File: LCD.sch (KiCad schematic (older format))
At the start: 5 parts

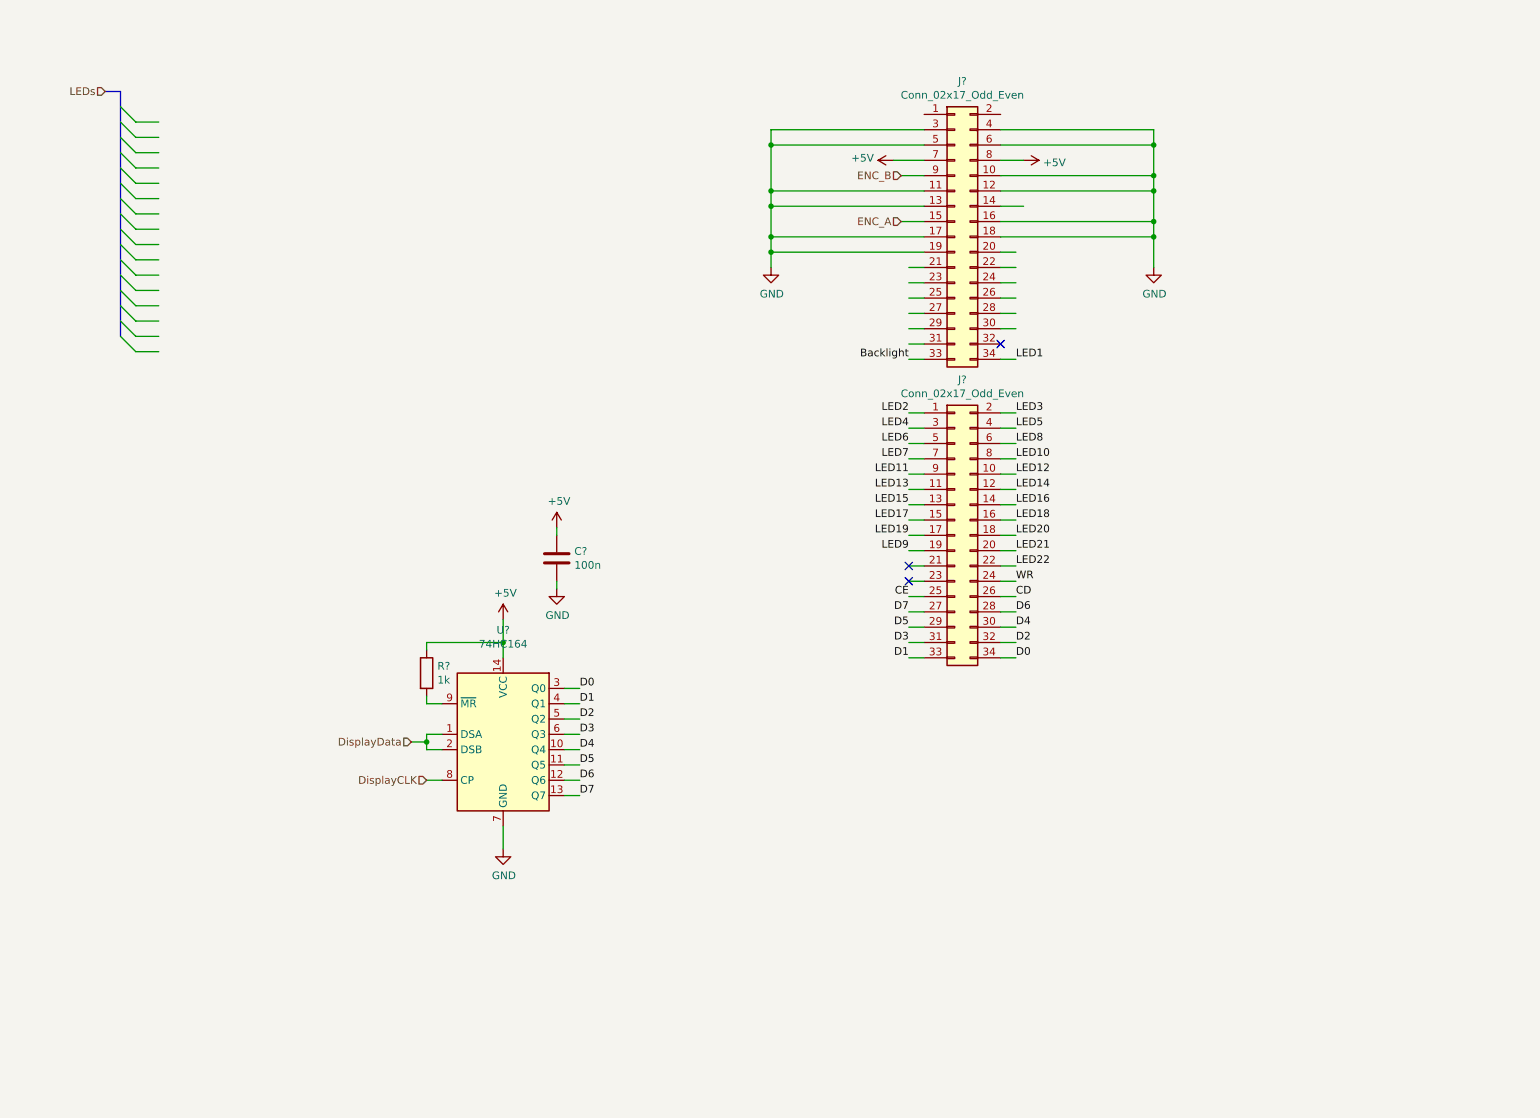
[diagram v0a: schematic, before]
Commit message: added rj45 input
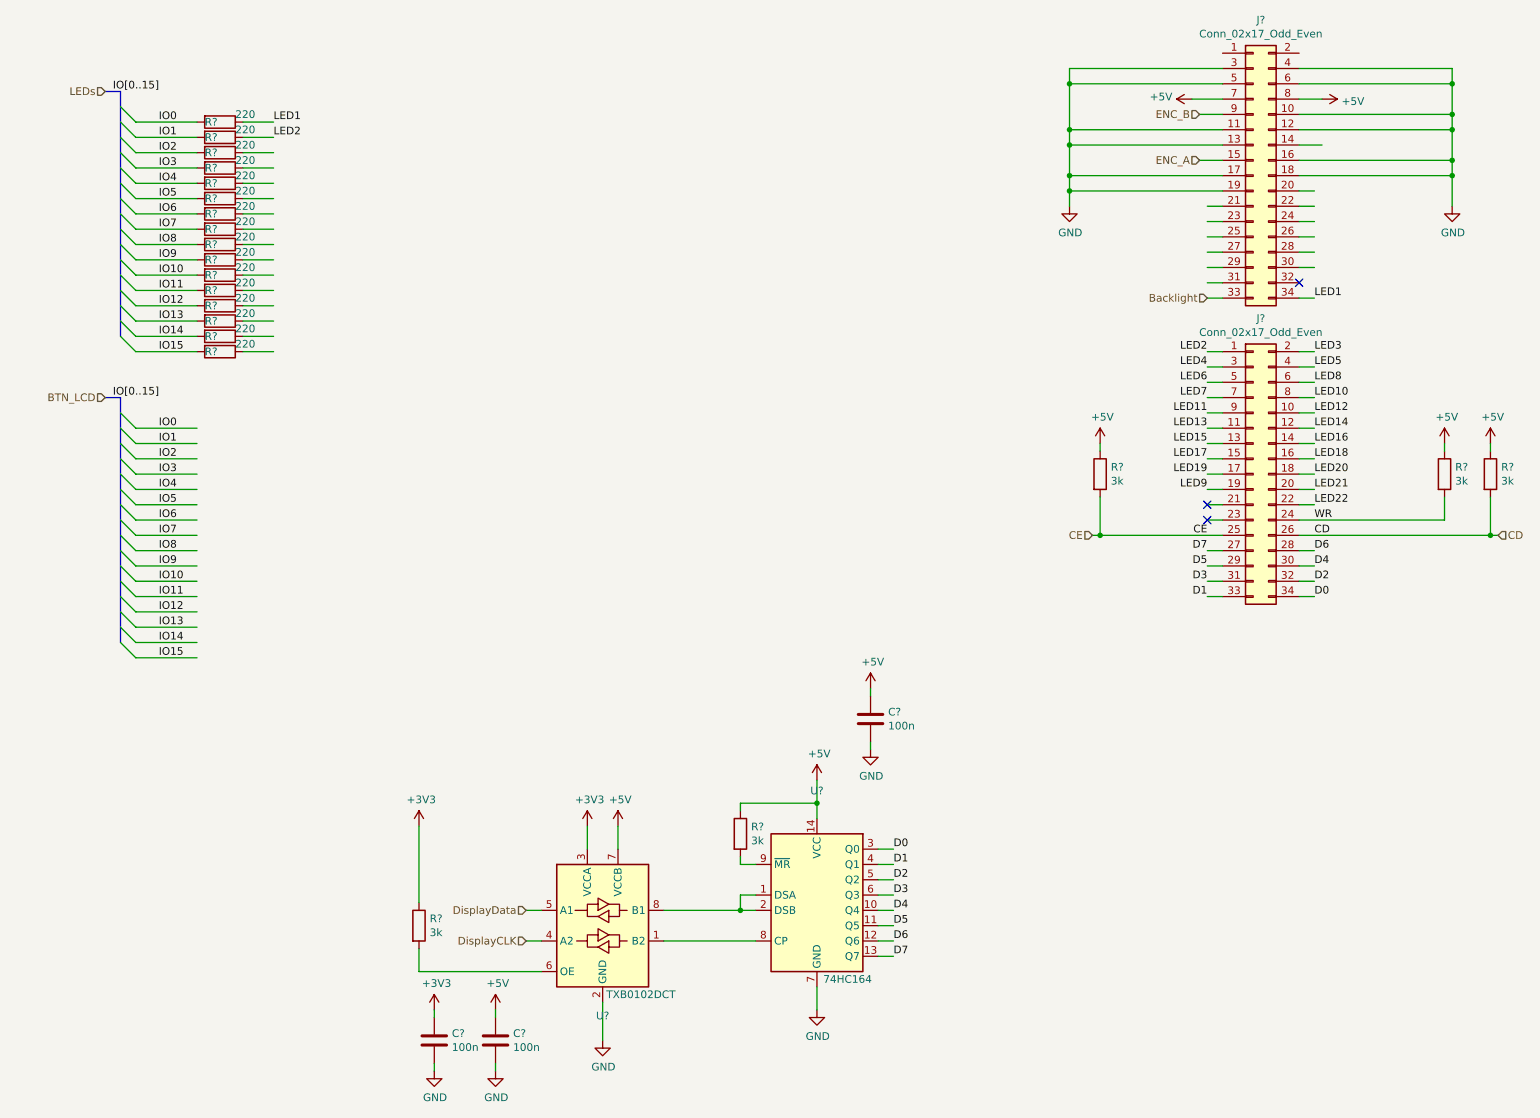
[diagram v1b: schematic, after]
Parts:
- added C? (x2): 100n, symbol AR2ISS:C
- added R? (x4): 3k, symbol AR2ISS:R
- added R? (x16): 220, symbol AR2ISS:R
- added U?: TXB0102DCT, Package_SO:TSSOP-8_3x3mm_P0.65mm, symbol Logic_LevelTranslator:TXB0102DCT
- R?: value 1k -> 3k
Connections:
- net labels added: +3V3, BTN_LCD, IO0, IO1, IO10, IO11, IO12, IO13, IO14, IO15, IO2, IO3, IO4, IO5, IO6, IO7, IO8, IO9, IO[0..15]
- wire segments 116 -> 167
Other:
- moved on the sheet: C?, J?, R?, U?

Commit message: Ready for layout
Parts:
- R? (x4): value 3k -> 10k
- gave numbers to parts that had none: 1
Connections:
- net labels added: LED_G, LED_R, SW_COL1, SW_COL2, SW_COL3, SW_COL4, SW_COL5, SW_ROW1, SW_ROW2, SW_ROW3, SW_ROW4, SW_ROW5
- wire segments 167 -> 166
- no-connect marks 3 -> 6
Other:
- moved on the sheet: R?
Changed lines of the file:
@@
 $Descr A4 11693 8268
 encoding utf-8
-Sheet 5 7
+Sheet 4 9
 Title ""
 Date ""
@@
 	8850 2200 8950 2200
 Wire Wire Line
-	8850 2100 8950 2100
-Wire Wire Line
 	8850 2000 8950 2000
 Wire Wire Line
@@
 P 5200 6000
 F 0 "R?" H 5270 6046 50  0000 L CNN
-F 1 "3k" H 5270 5955 50  0000 L CNN
+F 1 "10k" H 5270 5955 50  0000 L CNN
 F 2 "" V 5130 6000 50  0001 C CNN
 F 3 "~" H 5200 6000 50  0001 C CNN
@@
 Connection ~ 5200 6500
 $Comp
-L AR2ISS:R R?
+L AR2ISS:R 10k
 U 1 1 60905862
 P 3100 6600
-F 0 "R?" H 3170 6646 50  0000 L CNN
+F 0 "10k" H 3170 6646 50  0000 L CNN
 F 1 "3k" H 3170 6555 50  0000 L CNN
 F 2 "" V 3030 6600 50  0001 C CNN
@@
 P 9800 3650
 F 0 "R?" H 9870 3696 50  0000 L CNN
-F 1 "3k" H 9870 3605 50  0000 L CNN
+F 1 "10k" H 9870 3605 50  0000 L CNN
 F 2 "" V 9730 3650 50  0001 C CNN
 F 3 "~" H 9800 3650 50  0001 C CNN
@@
 P 10100 3650
 F 0 "R?" H 10170 3696 50  0000 L CNN
-F 1 "3k" H 10170 3605 50  0000 L CNN
+F 1 "10k" H 10170 3605 50  0000 L CNN
 F 2 "" V 10030 3650 50  0001 C CNN
 F 3 "~" H 10100 3650 50  0001 C CNN
@@
 L AR2ISS:R R?
 U 1 1 6096098F
-P 7550 3650
-F 0 "R?" H 7620 3696 50  0000 L CNN
-F 1 "3k" H 7620 3605 50  0000 L CNN
-F 2 "" V 7480 3650 50  0001 C CNN
-F 3 "~" H 7550 3650 50  0001 C CNN
-	1    7550 3650
-	1    0    0    -1
-$EndComp
-Wire Wire Line
-	7550 4050 8350 4050
-Wire Wire Line
-	7550 3800 7550 4050
-$Comp
-L power:+5V #PWR?
-U 1 1 609783F2
-P 7550 3450
-F 0 "#PWR?" H 7550 3300 50  0001 C CNN
-F 1 "+5V" H 7565 3623 50  0000 C CNN
-F 2 "" H 7550 3450 50  0001 C CNN
-F 3 "" H 7550 3450 50  0001 C CNN
-	1    7550 3450
-	1    0    0    -1
-$EndComp
-Wire Wire Line
-	7550 3450 7550 3500
+P 7550 4300
+F 0 "R?" H 7620 4346 50  0000 L CNN
+F 1 "10k" H 7620 4255 50  0000 L CNN
+F 2 "" V 7480 4300 50  0001 C CNN
+F 3 "~" H 7550 4300 50  0001 C CNN
+	1    7550 4300
+	1    0    0    -1
+$EndComp
 $Comp
 L power:+5V #PWR?
@@
 Text HLabel 8250 2500 0    50   Input ~ 0
 Backlight
-Wire Wire Line
-	7550 4050 7500 4050
+Text Label 2150 1550 0    50   ~ 0
+LED3
+Text Label 2150 1650 0    50   ~ 0
+LED7
+Text Label 2150 1750 0    50   ~ 0
+LED11
+Text Label 2150 1850 0    50   ~ 0
+LED12
+Text Label 2150 1950 0    50   ~ 0
+LED13
+Text Label 2150 2050 0    50   ~ 0
+LED14
+Text Label 2150 2150 0    50   ~ 0
+LED15
+Text Label 2150 2250 0    50   ~ 0
+LED17
+Text Label 2150 2350 0    50   ~ 0
+LED18
+Text Label 2150 2450 0    50   ~ 0
+LED19
+Text Label 2150 2550 0    50   ~ 0
+LED22
+Text Label 2150 2650 0    50   ~ 0
+LED_R
+Text Label 2150 2750 0    50   ~ 0
+LED_G
+Text Label 8250 1900 2    50   ~ 0
+SW_ROW1
+Text Label 8950 1900 0    50   ~ 0
+SW_ROW2
+Text Label 8250 2000 2    50   ~ 0
+SW_ROW3
+Text Label 8950 2000 0    50   ~ 0
+SW_ROW4
+Text Label 8250 2200 2    50   ~ 0
+SW_COL1
+Text Label 8950 2200 0    50   ~ 0
+SW_COL2
+Text Label 8250 2300 2    50   ~ 0
+SW_COL3
+Text Label 8950 2300 0    50   ~ 0
+SW_COL4
+Text Label 8250 2400 2    50   ~ 0
+SW_COL5
+Text Label 8250 2100 2    50   ~ 0
+SW_ROW5
+NoConn ~ 8850 2100
+NoConn ~ 8850 900
+NoConn ~ 8350 900
+Wire Wire Line
+	7500 4050 7550 4050
+Wire Wire Line
+	7550 4050 7550 4150
+Connection ~ 7550 4050
+Wire Wire Line
+	7550 4050 8350 4050
+Wire Wire Line
+	7550 4550 7550 4450
+$Comp
+L power:GND #PWR?
+U 1 1 606D63F1
+P 7550 4550
+F 0 "#PWR?" H 7550 4300 50  0001 C CNN
+F 1 "GND" H 7555 4377 50  0000 C CNN
+F 2 "" H 7550 4550 50  0001 C CNN
+F 3 "" H 7550 4550 50  0001 C CNN
+	1    7550 4550
+	1    0    0    -1
+$EndComp
+Text Label 1650 3350 0    50   ~ 0
+SW_ROW1
+Text Label 1650 3450 0    50   ~ 0
+SW_ROW2
+Text Label 1650 3550 0    50   ~ 0
+SW_ROW3
+Text Label 1650 3650 0    50   ~ 0
+SW_ROW4
+Text Label 1650 3750 0    50   ~ 0
+SW_ROW5
+Text Label 1650 4150 0    50   ~ 0
+SW_COL1
+Text Label 1650 4250 0    50   ~ 0
+SW_COL2
+Text Label 1650 4350 0    50   ~ 0
+SW_COL3
+Text Label 1650 4450 0    50   ~ 0
+SW_COL4
+Text Label 1650 4550 0    50   ~ 0
+SW_COL5
 Wire Bus Line
 	1150 3150 1150 4750
 Wire Bus Line
 	1150 1150 1150 2750
-Connection ~ 7550 4050
 $EndSCHEMATC

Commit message: first layout
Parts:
- removed R?: 220, symbol AR2ISS:R
- C15, C16, C17: renamed from C?; footprint (none) -> Capacitor_SMD:C_0603_1608Metric
- J3, J4: renamed from J?; footprint (none) -> Connector_IDC:IDC-Header_2x17_P2.54mm_Vertical
- R16, R17, R18, R19, R20, R21, R22, R23, R24, R25, R26, R27, R28, R29, R30, R33, R34, R35, R36: renamed from R?; footprint (none) -> Resistor_SMD:R_0603_1608Metric
- R32: renamed from 10k; footprint (none) -> Resistor_SMD:R_0603_1608Metric
- U10: renamed from U?; footprint (none) -> Package_SO:SOIC-14_3.9x8.7mm_P1.27mm
- gave numbers to parts that had none: 1
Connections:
- net labels added: BTN0, BTN1, BTN10, BTN11, BTN12, BTN13, BTN14, BTN15, BTN2, BTN3, BTN4, BTN5, BTN6, BTN7, BTN8, BTN9, BTN[0..15], LEDs0, LEDs1, LEDs10, LEDs11, LEDs12, LEDs13, LEDs14, LEDs15, LEDs2, LEDs3, LEDs4, LEDs5, LEDs6, LEDs7, LEDs8, LEDs9, LEDs[0..15]
- net labels removed: BTN_LCD, IO0, IO1, IO10, IO11, IO12, IO13, IO14, IO15, IO2, IO3, IO4, IO5, IO6, IO7, IO8, IO9, IO[0..15], LEDs
- wire segments 166 -> 165
